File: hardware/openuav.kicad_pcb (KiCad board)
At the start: 4 copper layers, 36 x 36 mm, 85 parts, among them J1 Conn_01x01, J10 Conn_01x01, J11 Conn_01x01, J12 Conn_01x01, J13 Conn_01x01, J14 Conn_01x01, J15 Conn_01x01, J16 Conn_01x01, J17 Conn_01x01, J18 Conn_01x01, J19 Conn_01x01, J2 Conn_01x01, J20 Conn_01x01, J21 Conn_01x01, J22 Conn_01x01, J23 Conn_01x01, J24 Conn_01x01, J25 Conn_01x01, J3 Conn_01x01, J4 Conn_01x01, J5 Conn_01x01, J6 Conn_01x01, J7 Conn_01x01, J8 Conn_01x01, J9 Conn_01x01, J99 USB_C_Receptacle_USB2.0, SW1 SW_Push, SW2 SW_Push, U1 STM32G431CBUx, U2 LPS22HH, U3 LSM6DSR, U4 SY8303, U5 SY8303, U6 W25N01GVZEIG, U7 TLV75733PDBV

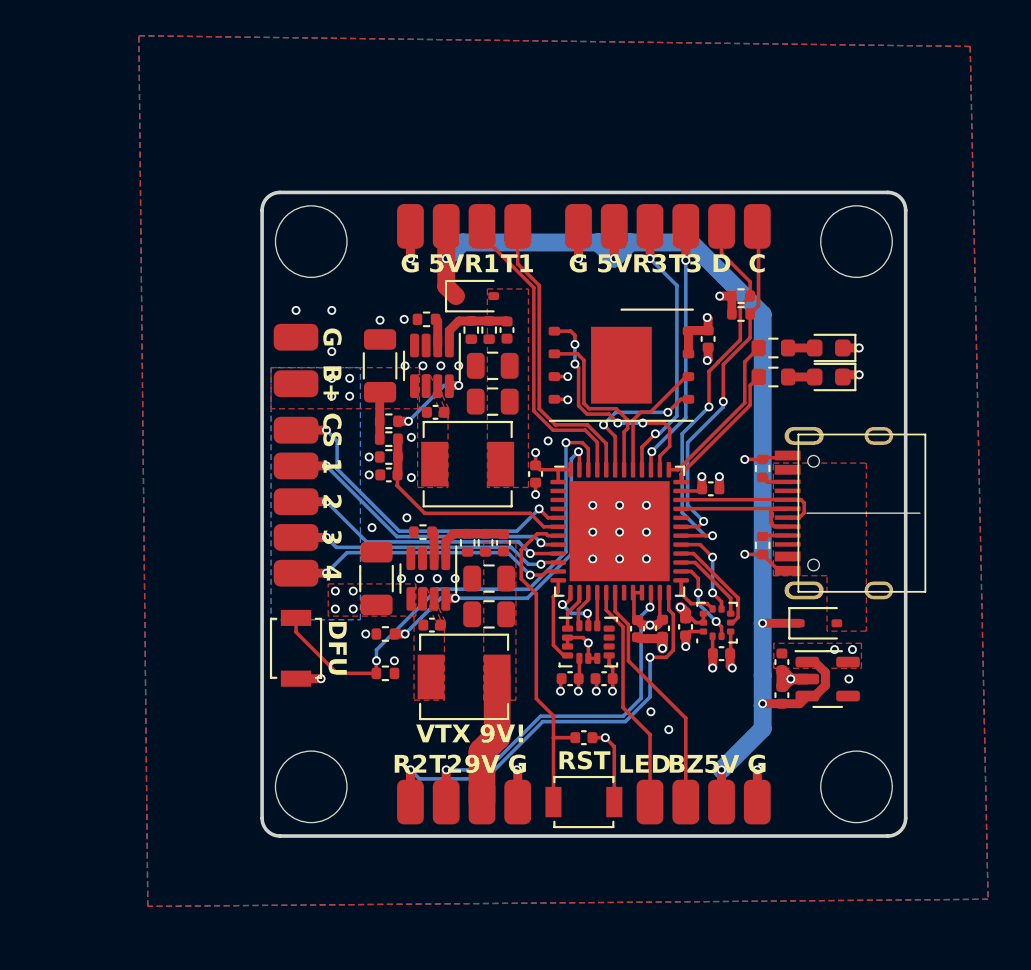
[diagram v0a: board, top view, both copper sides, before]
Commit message: Remove SMPS in preparation for next attempt
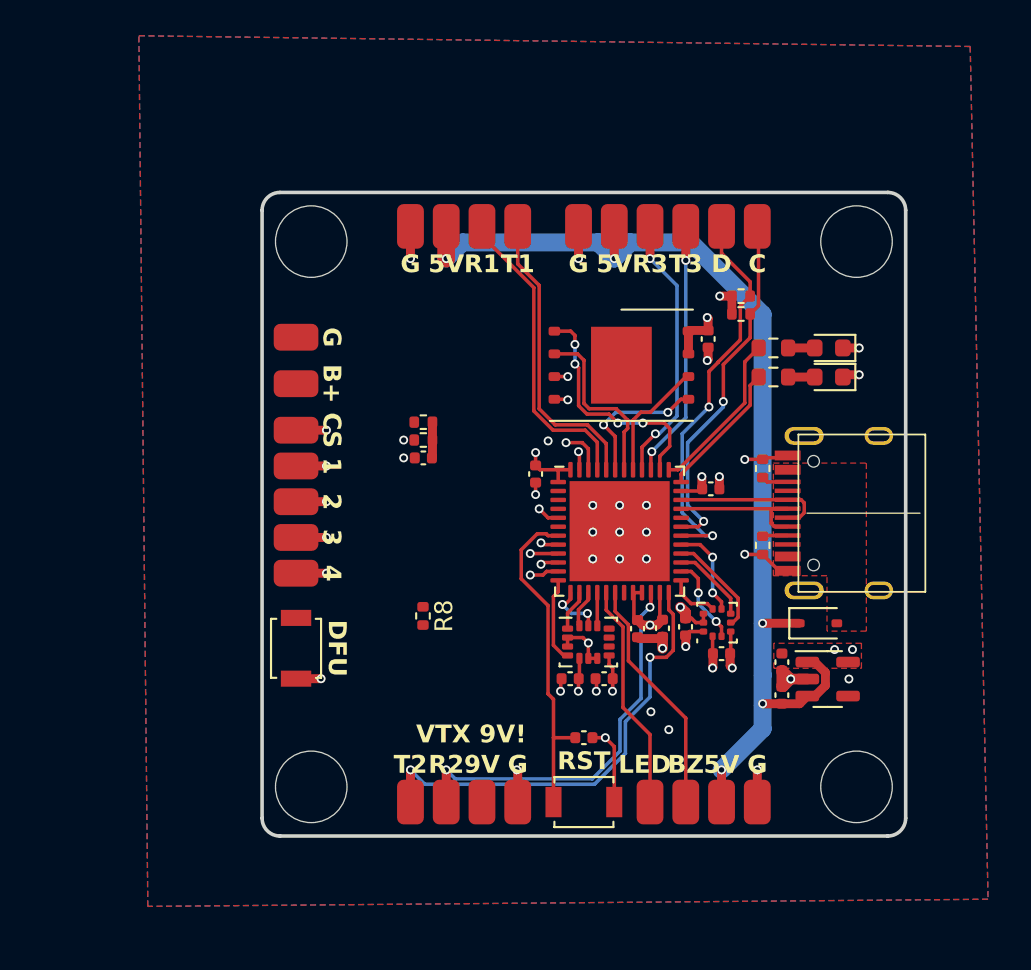
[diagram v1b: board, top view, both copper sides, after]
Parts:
- removed C10, C2: 10u, Capacitor_SMD:C_1206_3216Metric
- removed C15, C8: 10n, Capacitor_SMD:C_0402_1005Metric
- removed C17, C20, C21, C9: 22u, Capacitor_SMD:C_0805_2012Metric
- removed C18, C19: 100p, Capacitor_SMD:C_0402_1005Metric
- removed D4: PMEG2020AEA, Diode_SMD:D_SOD-323
- removed L1, L2: 6.8u, Inductor_SMD:L_Sunlord_MWSA0402S
- removed R13, R3: 47k, Resistor_SMD:R_0402_1005Metric
- removed R14, R4: 100k, Resistor_SMD:R_0402_1005Metric
- removed R15: 7.15k, Resistor_SMD:R_0402_1005Metric
- removed R16, R17: 10k, Resistor_SMD:R_0402_1005Metric
- removed R5: 13.7k, Resistor_SMD:R_0402_1005Metric
- removed U4, U5: SY8303, Package_TO_SOT_SMD:TSOT-23-8
- moved R8 3.84 mm to (139.0, 73.7), turned to -90 degrees
- moved C14 2.15 mm to (139.0, 64.8)
- moved R12 2.15 mm to (139.0, 62.9)
- moved R6 2.15 mm to (139.0, 63.9)
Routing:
- net BOOT0: track 29.1 -> 2.57 mm, vias 2 -> 1
- net 9VEN: track 19.1 -> 1.03 mm, vias 3 -> 1
- net CURRENT: track 18.7 -> 2.97 mm
- net PWM_1: track 16.5 -> 2.70 mm
- net PWM_3: track 15.3 -> 2.70 mm
- net PWM_2: track 15.9 -> 3.26 mm
- net PWM_4: track 15.7 -> 3.35 mm
- net VOLTAGE: track 12.6 -> 2.01 mm
- net +9V: track 7.35 -> 0.00 mm
- net Net-(U4-EN): track 4.63 -> 0.00 mm, vias 2 -> 0
- net Net-(U5-FB): track 4.36 -> 0.00 mm
- net Net-(U4-FB): track 4.30 -> 0.00 mm
- net +BATT: track 2.63 -> 0.00 mm, vias 8 -> 0
- net +5V: track 64.4 -> 62.1 mm
- net Net-(U5-FS): track 1.51 -> 0.00 mm
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- removed copper zone on F.Cu, net +9V
- removed copper zone on B.Cu, net +BATT
- removed copper zone on F.Cu, net +BATT
- removed copper zone on F.Cu, net Net-(D4-A)
- removed copper zone on F.Cu, net Net-(U4-BS)
- removed copper zone on F.Cu, net Net-(U4-LX)
- removed copper zone on F.Cu, net Net-(U5-BS)
- removed copper zone on F.Cu, net Net-(U5-LX)

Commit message: Begin TI SMPS design
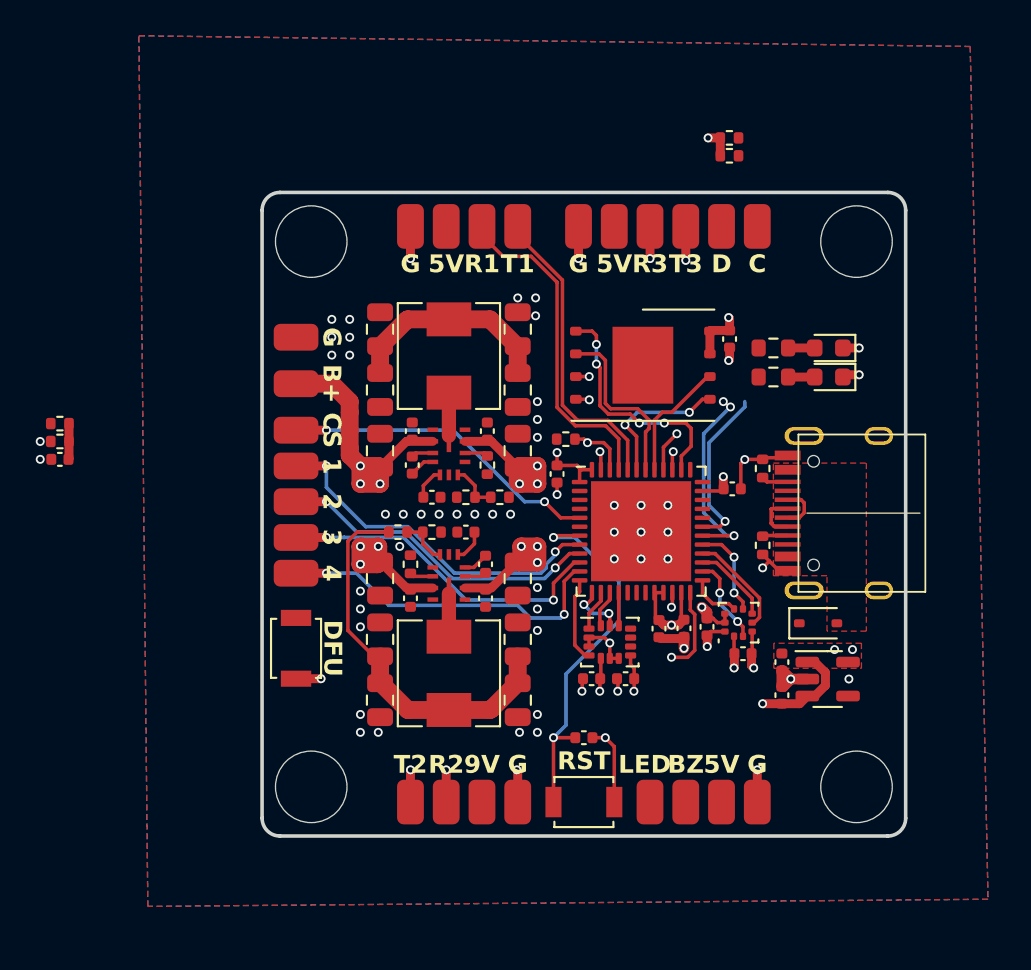
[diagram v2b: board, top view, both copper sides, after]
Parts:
- added C10: 22u, Capacitor_SMD:C_0805_2012Metric, F.Cu at (136.6, 75.0)
- added C10: 22u, Capacitor_SMD:C_0805_2012Metric, F.Cu at (144.3, 61.0)
- added C15: 22u, Capacitor_SMD:C_0805_2012Metric, F.Cu at (136.6, 61.0)
- added C15: 22u, Capacitor_SMD:C_0805_2012Metric, F.Cu at (144.3, 75.0)
- added C17: 10u, Capacitor_SMD:C_0805_2012Metric, F.Cu at (136.6, 71.6)
- added C17: 10u, Capacitor_SMD:C_0805_2012Metric, F.Cu at (144.3, 64.5)
- added C18: 10u, Capacitor_SMD:C_0805_2012Metric, F.Cu at (136.6, 64.5)
- added C18: 10u, Capacitor_SMD:C_0805_2012Metric, F.Cu at (144.3, 71.6)
- added C19: 100n, Capacitor_SMD:C_0402_1005Metric, F.Cu at (142.6, 63.4)
- added C19: 100n, Capacitor_SMD:C_0402_1005Metric, F.Cu at (138.3, 72.7)
- added C2: 1u, Capacitor_SMD:C_0402_1005Metric, F.Cu at (141.4, 69.0)
- added C2: 1u, Capacitor_SMD:C_0402_1005Metric, F.Cu at (139.5, 67.0)
- added C20: 22u, Capacitor_SMD:C_0805_2012Metric, F.Cu at (136.6, 57.6)
- added C20: 22u, Capacitor_SMD:C_0805_2012Metric, F.Cu at (144.3, 78.4)
- added C21: 100n, Capacitor_SMD:C_0402_1005Metric, F.Cu at (142.5, 72.7)
- added C21: 100n, Capacitor_SMD:C_0402_1005Metric, F.Cu at (138.4, 63.4)
- added C22: 22u, Capacitor_SMD:C_0805_2012Metric, F.Cu at (144.3, 57.6)
- added C22: 22u, Capacitor_SMD:C_0805_2012Metric, F.Cu at (136.6, 78.4)
- added C9: 100n, Capacitor_SMD:C_0402_1005Metric, F.Cu at (142.5, 70.8)
- added C9: 100n, Capacitor_SMD:C_0402_1005Metric, F.Cu at (138.4, 65.2)
- added L1: 6.8u, Inductor_SMD:L_Sunlord_MWSA0503S, F.Cu at (140.4, 76.9)
- added L1: 6.8u, Inductor_SMD:L_Sunlord_MWSA0503S, F.Cu at (140.4, 59.1)
- added R3: 2.44k, Resistor_SMD:R_0402_1005Metric, F.Cu at (141.4, 67.0)
- added R3: 2.44k, Resistor_SMD:R_0402_1005Metric, F.Cu at (139.5, 69.0)
- added R4: 22k, Resistor_SMD:R_0402_1005Metric, F.Cu at (137.6, 69.0)
- added R4: 22k, Resistor_SMD:R_0402_1005Metric, F.Cu at (143.3, 67.0)
- added R5: 10k, Resistor_SMD:R_0402_1005Metric, F.Cu at (142.6, 65.2)
- added R5: 10k, Resistor_SMD:R_0402_1005Metric, F.Cu at (138.3, 70.8)
- added U4: ~, footprints:RNX0012B, F.Cu at (140.4, 64.4)
- added U4: ~, footprints:RNX0012B, F.Cu at (140.4, 71.7)
- moved C14 20.3 mm to (118.7, 64.9)
- moved R12 20.3 mm to (118.7, 62.9)
- moved R6 20.3 mm to (118.7, 63.9)
- moved R8 12.7 mm to (147.0, 63.8), turned to 180 degrees
- moved R10 8.87 mm to (156.1, 48.0)
- moved R9 8.87 mm to (156.1, 47.0)
- moved C11 1.20 mm to (148.4, 77.2)
- moved C13 1.20 mm to (156.9, 75.8)
- moved C16 1.20 mm to (156.2, 58.2)
- moved C3 1.20 mm to (150.3, 77.2)
- moved C5 1.20 mm to (156.3, 66.6)
- moved U2 1.20 mm to (156.7, 74.1)
- moved U6 1.20 mm to (151.3, 59.7)
- moved C12 1.20 mm to (154.9, 74.3)
- moved C4 1.20 mm to (146.5, 65.8)
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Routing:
- net +5V: track 62.1 -> 5.91 mm, vias 5 -> 1
- net +BATT: track 0.00 -> 37.6 mm, vias 0 -> 12
- net Net-(C10-Pad1): track 0.00 -> 33.8 mm
- net UART_4_RX: track 22.0 -> 2.63 mm
- net UART_4_TX: track 25.6 -> 6.59 mm
- net PWM_1: track 2.70 -> 19.9 mm
- net PWM_3: track 2.70 -> 18.7 mm
- net PWM_4: track 3.35 -> 19.1 mm
- net PWM_2: track 3.26 -> 18.2 mm
- net CURRENT: track 2.97 -> 17.9 mm
- net PWM_6: track 13.3 -> 0.00 mm
- net PWM_5: track 12.7 -> 0.00 mm
- net I2C_SDA: track 22.2 -> 10.5 mm
- net UART_3_TX: track 14.4 -> 2.93 mm
- net UART_3_RX: track 15.2 -> 4.12 mm
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- added copper zone on In2.Cu, net +BATT
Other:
- board text removed: "VTX 9V!"

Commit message: Work in progress new SMPS
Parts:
- removed the C10 at (144.3, 61.0)
- removed the C15 at (136.6, 61.0)
- removed the C17 at (144.3, 64.5)
- removed the C18 at (136.6, 64.5)
- removed the C19 at (142.6, 63.4)
- removed the C2 at (139.5, 67.0)
- removed the C20 at (136.6, 57.6)
- removed the C20 at (144.3, 78.4)
- removed the C21 at (138.4, 63.4)
- removed the C22 at (144.3, 57.6)
- removed the C22 at (136.6, 78.4)
- removed the C9 at (138.4, 65.2)
- removed the L1 at (140.4, 59.1)
- removed the R3 at (141.4, 67.0)
- removed the R4 at (143.3, 67.0)
- removed R5 (x2): 10k, Resistor_SMD:R_0402_1005Metric
- removed SW2: SW_Push, Button_Switch_SMD:SW_SPST_B3U-1000P
- removed the U4 at (140.4, 64.4)
- added C20: 10u, Capacitor_SMD:C_1206_3216Metric, F.Cu at (144.3, 63.4)
- added C22: 100n, Capacitor_SMD:C_0402_1005Metric, F.Cu at (142.6, 63.3)
- added C23: 10u, Capacitor_SMD:C_1206_3216Metric, F.Cu at (136.2, 63.3)
- added C26: 1u, Capacitor_SMD:C_0402_1005Metric, F.Cu at (139.3, 66.8)
- added C27: 100n, Capacitor_SMD:C_0402_1005Metric, F.Cu at (137.9, 65.2)
- added C28: 22u, Capacitor_SMD:C_1206_3216Metric, F.Cu at (144.3, 58.7)
- added C29: 22u, Capacitor_SMD:C_1206_3216Metric, F.Cu at (136.2, 58.7)
- added C30: 1u, Capacitor_SMD:C_0402_1005Metric, F.Cu at (150.3, 78.2)
- added C31: 1u, Capacitor_SMD:C_0402_1005Metric, F.Cu at (154.1, 79.6)
- added C32: 1u, Capacitor_SMD:C_0402_1005Metric, F.Cu at (154.1, 77.8)
- added C33: 10u, Capacitor_SMD:C_0603_1608Metric, F.Cu at (148.7, 55.5)
- added C34: 10u, Capacitor_SMD:C_0603_1608Metric, F.Cu at (147.6, 79.2)
- added C35: 10u, Capacitor_SMD:C_0603_1608Metric, F.Cu at (161.1, 61.6)
- added C8: 100n, Capacitor_SMD:C_0402_1005Metric, F.Cu at (137.9, 63.3)
- added D4: PMEG2020AEA, Diode_SMD:D_SOD-323, F.Cu at (133.3, 58.1)
- added FB1: FerriteBead, Inductor_SMD:L_0805_2012Metric, F.Cu at (151.8, 79.7)
- added L2: 10u, Inductor_SMD:L_Sunlord_MWSA0503S, F.Cu at (140.2, 59.1)
- added R13: 10k, Resistor_SMD:R_0402_1005Metric, F.Cu at (146.6, 63.6)
- added R14: 22k, Resistor_SMD:R_0402_1005Metric, F.Cu at (142.6, 66.3)
- added R15: 2.44k, Resistor_SMD:R_0402_1005Metric, F.Cu at (141.2, 66.8)
- added U5: ~, footprints:RNX0012B, F.Cu at (140.2, 64.3)
- added U8: TLV75733PDBV, Package_TO_SOT_SMD:SOT-23-5, F.Cu at (156.7, 78.8)
- C10, C15, C17, C18: footprint Capacitor_SMD:C_0805_2012Metric -> Capacitor_SMD:C_1206_3216Metric
- J15, J16: footprint footprints:smallpad -> footprints:largepad
- L1: value 6.8u -> 10u
- moved R6 27.7 mm to (146.1, 67.6), turned to 0 degrees
- moved C14 27.5 mm to (146.1, 66.6), turned to 0 degrees
- moved R12 26.9 mm to (145.0, 68.5)
- moved SW1 18.3 mm to (148.0, 84.1), turned to 180 degrees
- moved R8 17.0 mm to (145.4, 80.7), turned to 90 degrees
- moved R10 8.31 mm to (156.6, 56.2)
- moved R9 8.31 mm to (156.6, 55.2)
- moved J18 5.80 mm to (131.9, 69.1)
- moved J22 5.80 mm to (131.9, 71.1)
- moved J23 5.80 mm to (131.9, 73.1)
- moved J24 5.80 mm to (131.9, 75.1)
- moved J25 5.80 mm to (131.9, 77.1)
- moved J15 4.62 mm to (131.9, 65.3)
- moved C1 3.89 mm to (146.9, 76.8), turned to 90 degrees
- moved J16 3.23 mm to (131.9, 61.3)
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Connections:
- C10 pad 1: Net-(C10-Pad1) -> +9V
- C15 pad 1: Net-(C10-Pad1) -> +9V
- C3 pad 1: +3V3 -> VDDA
- L1 pad 2: Net-(C10-Pad1) -> +9V
- R4 pad 1: Net-(C10-Pad1) -> +9V
- U3 pad 8: +3V3 -> VDDA
- U4 pad 9: 10VEN -> 9VEN
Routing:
- net +5V: track 5.91 -> 89.5 mm, vias 1 -> 7
- net +BATT: track 37.6 -> 0.00 mm, vias 12 -> 16
- net Net-(C10-Pad1): track 33.8 -> 0.00 mm
- net BOOT0: track 3.35 -> 30.8 mm, vias 1 -> 2
- net +9V: track 0.00 -> 25.5 mm, vias 0 -> 2
- net UART_4_RX: track 2.63 -> 23.2 mm
- net UART_4_TX: track 6.59 -> 26.9 mm
- net Net-(D4-A): track 0.00 -> 19.7 mm, vias 0 -> 2
- net 9VEN: track 1.03 -> 19.5 mm, vias 1 -> 2
- net PWM_6: track 0.00 -> 12.9 mm
- net PWM_5: track 0.00 -> 12.2 mm
- net NRST: track 21.3 -> 9.07 mm, vias 2 -> 0
- net UART_3_TX: track 2.93 -> 14.8 mm
- net UART_3_RX: track 4.12 -> 15.7 mm
- net I2C_SDA: track 10.5 -> 21.9 mm
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- added copper zone on F.Cu, net +BATT
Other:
- board text removed: "RST"
